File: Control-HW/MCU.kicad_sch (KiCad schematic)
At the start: 6 parts

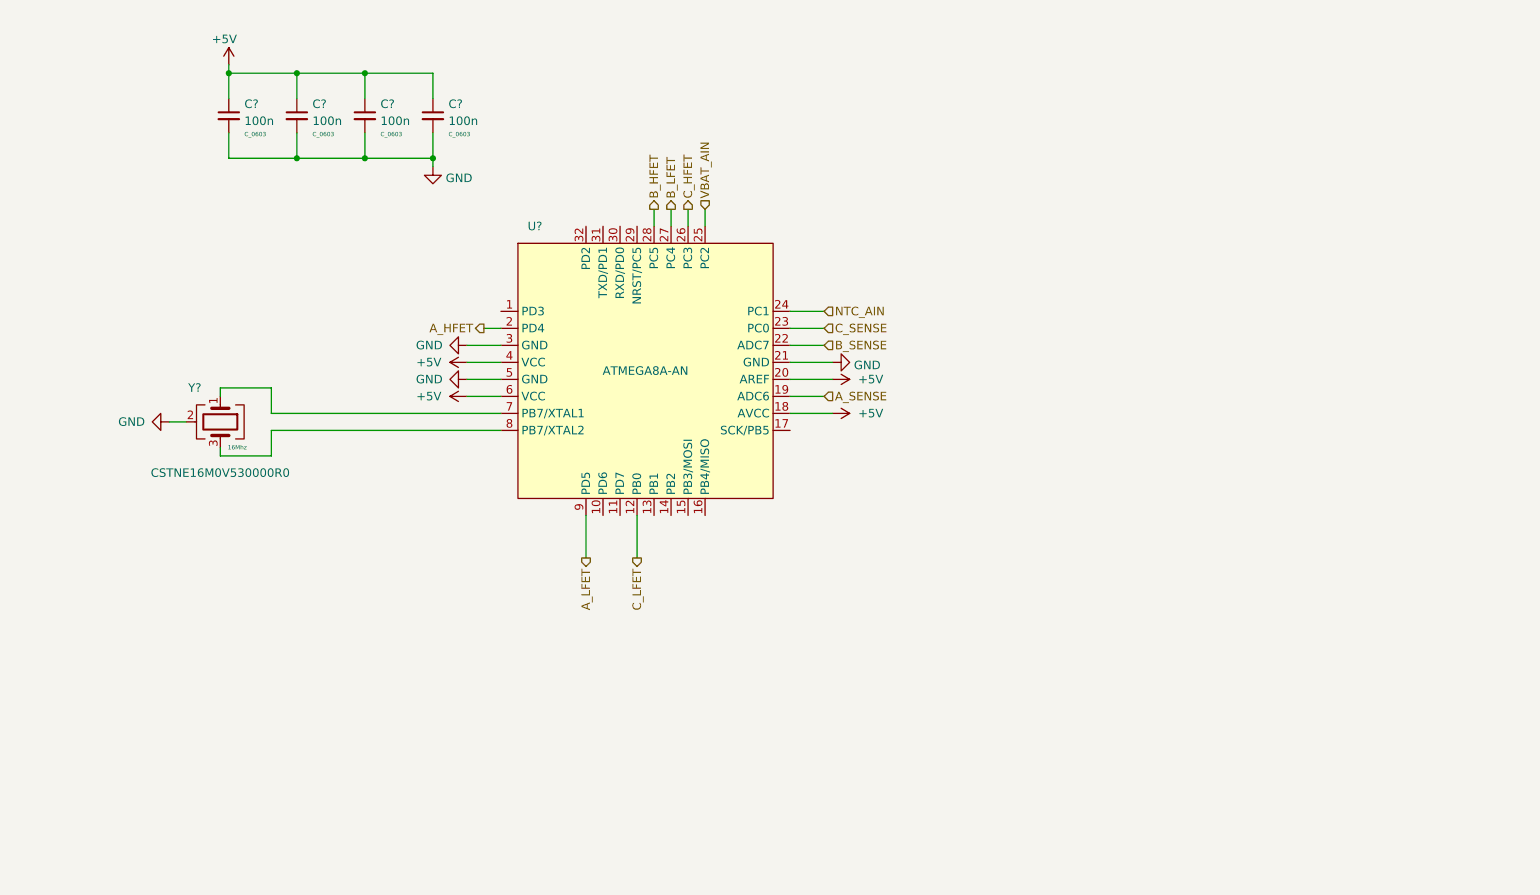
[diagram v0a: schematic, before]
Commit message: Assign pinout for MCU
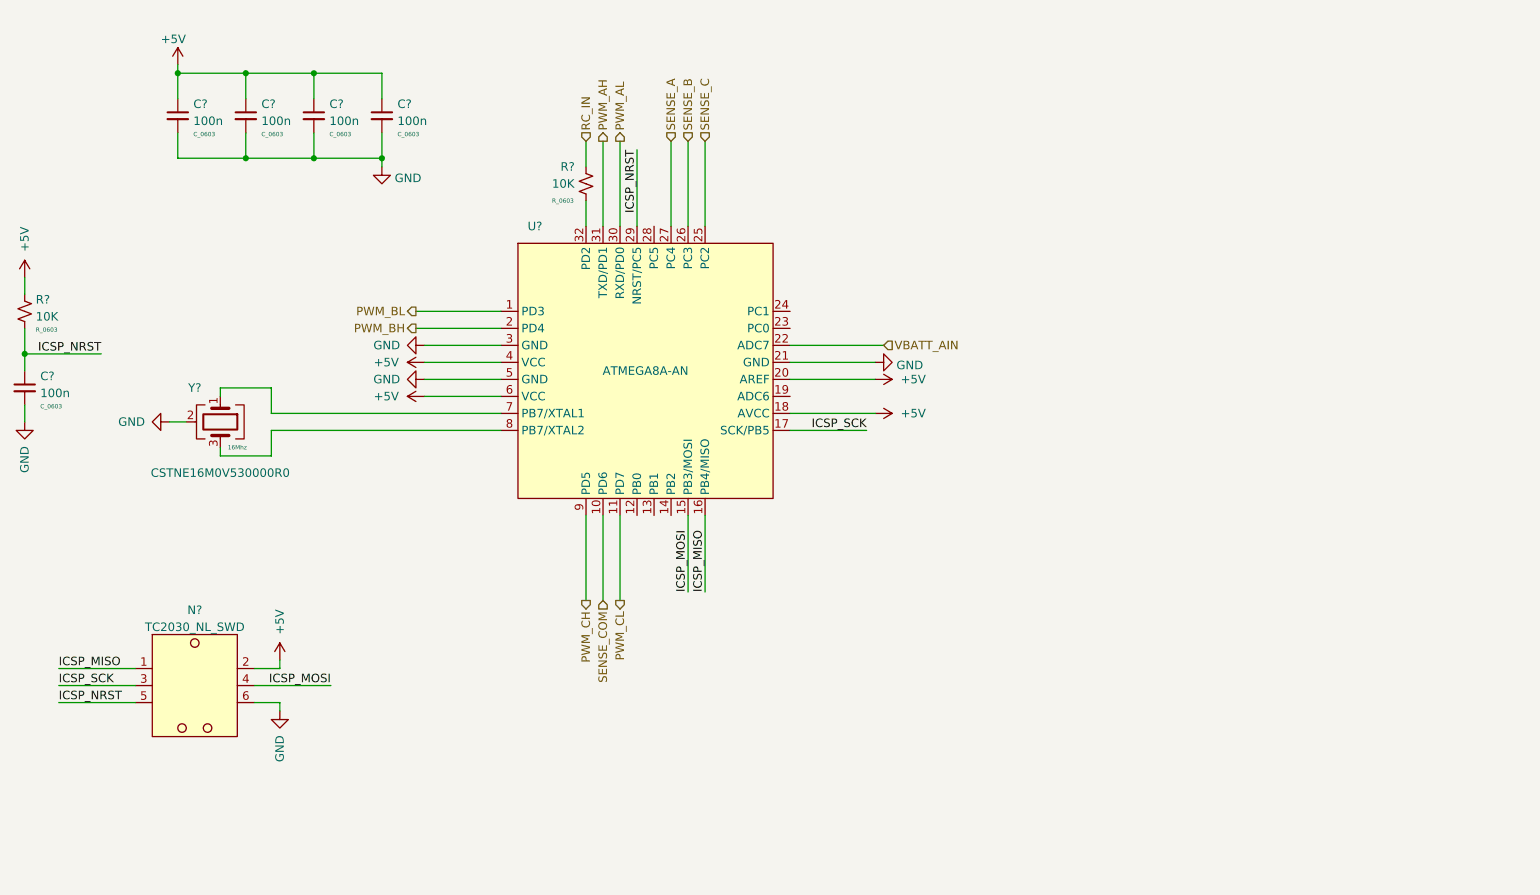
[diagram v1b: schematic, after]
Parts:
- added C?: 100n, C_Capacitor:C_0603, symbol C_Capacitor:C_0603
- added N?: TC2030_NL_SWD, N_NonPart:TagConnect_2030_NL, symbol N_NonPart:TC2030_NL_SWD
- added R? (x2): 10K, R_Resistor:R_0603, symbol R_Resistor:R_0603
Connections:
- net +5V: now also N?.2, R?.1
- net GND: now also C?.2, N?.6
- net PWM_BL: now reaches U?.1 (PD3)
- net SENSE_COM: now reaches U?.10 (PD6)
- net PWM_CL: now reaches U?.11 (PD7)
- net ICSP_MOSI: now reaches U?.15 (PB3/MOSI)
- net ICSP_MOSI: now also N?.4
- net ICSP_MISO: now reaches U?.16 (PB4/MISO)
- net ICSP_MISO: now also N?.1
- net ICSP_SCK: now reaches U?.17 (SCK/PB5)
- net ICSP_SCK: now also N?.3
- net ICSP_NRST: now reaches U?.29 (NRST/PC5)
- net ICSP_NRST: now also C?.1, N?.5, R?.2
- net PWM_AL: now reaches U?.30 (RXD/PD0)
- net PWM_AH: now reaches U?.31 (TXD/PD1)
- net at U?.32 (PD2): now also R?.2
- net A_HFET renamed PWM_BH
- net A_LFET renamed PWM_CH
- net A_SENSE: no longer names the net of U?.19 (ADC6)
- net B_HFET: no longer names the net of U?.28 (PC5)
- net B_LFET renamed SENSE_A
- net B_SENSE renamed VBATT_AIN
- net C_HFET renamed SENSE_B
- net C_LFET: no longer names the net of U?.12 (PB0)
- net C_SENSE: no longer names the net of U?.23 (PC0)
- net NTC_AIN: no longer names the net of U?.24 (PC1)
- net VBAT_AIN renamed SENSE_C
- new net RC_IN: R?.1
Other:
- moved on the sheet: C?

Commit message: First pass at control HW
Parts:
- removed C?: 100n, C_Capacitor:C_0603, symbol C_Capacitor:C_0603
- added C?: 10u, C_Capacitor:C_0805, symbol C_Capacitor:C_0805
- added C?: 100n, C_Capacitor:C_0603, symbol C_Capacitor:C_0603
- added R?: 2K, R_Resistor:R_0603, symbol R_Resistor:R_0603
- added R?: 47K, R_Resistor:R_0603, symbol R_Resistor:R_0603
- R?: value 10K -> 2K
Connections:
- net +5V: now also C?.1
- net GND: now also C?.2, C?.2, R?.2
- net VBATT_AIN: now also C?.1, R?.1, R?.2
- new net VBATT: R?.1
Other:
- note added: "4.08V @ 100V"
- moved on the sheet: C?, N?, R?, U?, Y?

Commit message: First revision
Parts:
- gave numbers to parts that had none: 13
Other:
- note added: "Pinout targeted to mirrow the rb70a.hex requirements"
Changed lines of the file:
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@@
+    (effects (font (size 1.27 1.27)) (justify left bottom))
+  )
+  (text "Pinout targeted to mirrow the rb70a.hex requirements"
+    (at 130.81 45.72 0)
     (effects (font (size 1.27 1.27)) (justify left bottom))
   )
@@
   (symbol (lib_id "power:GND") (at 46.99 101.6 0) (unit 1)
     (in_bom yes) (on_board yes)
-    (property "Reference" "#PWR?" (id 0) (at 46.99 107.95 0)
+    (property "Reference" "#PWR07" (id 0) (at 46.99 107.95 0)
       (effects (font (size 1.27 1.27)) hide)
     )
@@
   (symbol (lib_id "power:+5V") (at 46.99 80.01 0) (unit 1)
     (in_bom yes) (on_board yes)
-    (property "Reference" "#PWR?" (id 0) (at 46.99 83.82 0)
+    (property "Reference" "#PWR06" (id 0) (at 46.99 83.82 0)
       (effects (font (size 1.27 1.27)) hide)
     )
@@
   (symbol (lib_id "C_Capacitor:C_0805") (at 97.79 41.91 0) (unit 1)
     (in_bom yes) (on_board yes) (fields_autoplaced)
-    (property "Reference" "C?" (id 0) (at 100.1141 40.167 0)
+    (property "Reference" "C5" (id 0) (at 100.1141 40.167 0)
       (effects (font (size 1.27 1.27)) (justify left))
     )
@@
   (symbol (lib_id "N_NonPart:TC2030_NL_SWD") (at 69.85 147.32 0) (unit 1)
     (in_bom no) (on_board yes) (fields_autoplaced)
-    (property "Reference" "N?" (id 0) (at 69.85 136.051 0))
+    (property "Reference" "N6" (id 0) (at 69.85 136.051 0))
     (property "Value" "TC2030_NL_SWD" (id 1) (at 69.85 138.5879 0))
     (property "Footprint" "N_NonPart:TagConnect_2030_NL" (id 2) (at 69.85 158.75 0)
@@
   (symbol (lib_id "power:+5V") (at 123.19 93.98 90) (unit 1)
     (in_bom yes) (on_board yes)
-    (property "Reference" "#PWR?" (id 0) (at 127 93.98 0)
+    (property "Reference" "#PWR014" (id 0) (at 127 93.98 0)
       (effects (font (size 1.27 1.27)) hide)
     )
@@
   (symbol (lib_id "power:GND") (at 85.09 102.87 270) (unit 1)
     (in_bom yes) (on_board yes)
-    (property "Reference" "#PWR?" (id 0) (at 78.74 102.87 0)
+    (property "Reference" "#PWR011" (id 0) (at 78.74 102.87 0)
       (effects (font (size 1.27 1.27)) hide)
     )
@@
   (symbol (lib_id "power:GND") (at 228.6 99.06 0) (unit 1)
     (in_bom yes) (on_board yes)
-    (property "Reference" "#PWR?" (id 0) (at 228.6 105.41 0)
+    (property "Reference" "#PWR020" (id 0) (at 228.6 105.41 0)
       (effects (font (size 1.27 1.27)) hide)
     )
@@
   (symbol (lib_id "C_Capacitor:C_0603") (at 87.63 41.91 0) (unit 1)
     (in_bom yes) (on_board yes) (fields_autoplaced)
-    (property "Reference" "C?" (id 0) (at 89.9541 40.167 0)
+    (property "Reference" "C4" (id 0) (at 89.9541 40.167 0)
       (effects (font (size 1.27 1.27)) (justify left))
     )
@@
   (symbol (lib_id "power:+5V") (at 190.5 96.52 270) (unit 1)
     (in_bom yes) (on_board yes)
-    (property "Reference" "#PWR?" (id 0) (at 186.69 96.52 0)
+    (property "Reference" "#PWR018" (id 0) (at 186.69 96.52 0)
       (effects (font (size 1.27 1.27)) hide)
     )
@@
   (symbol (lib_id "power:+5V") (at 123.19 99.06 90) (unit 1)
     (in_bom yes) (on_board yes)
-    (property "Reference" "#PWR?" (id 0) (at 127 99.06 0)
+    (property "Reference" "#PWR016" (id 0) (at 127 99.06 0)
       (effects (font (size 1.27 1.27)) hide)
     )
@@
   (symbol (lib_id "power:GND") (at 82.55 151.13 0) (unit 1)
     (in_bom yes) (on_board yes)
-    (property "Reference" "#PWR?" (id 0) (at 82.55 157.48 0)
+    (property "Reference" "#PWR010" (id 0) (at 82.55 157.48 0)
       (effects (font (size 1.27 1.27)) hide)
     )
@@
   (symbol (lib_id "power:+5V") (at 82.55 143.51 0) (unit 1)
     (in_bom yes) (on_board yes)
-    (property "Reference" "#PWR?" (id 0) (at 82.55 147.32 0)
+    (property "Reference" "#PWR09" (id 0) (at 82.55 147.32 0)
       (effects (font (size 1.27 1.27)) hide)
     )
@@
   (symbol (lib_id "power:GND") (at 97.79 49.53 0) (unit 1)
     (in_bom yes) (on_board yes) (fields_autoplaced)
-    (property "Reference" "#PWR?" (id 0) (at 97.79 55.88 0)
+    (property "Reference" "#PWR012" (id 0) (at 97.79 55.88 0)
       (effects (font (size 1.27 1.27)) hide)
     )
@@
   (symbol (lib_id "power:GND") (at 190.5 93.98 90) (unit 1)
     (in_bom yes) (on_board yes) (fields_autoplaced)
-    (property "Reference" "#PWR?" (id 0) (at 196.85 93.98 0)
+    (property "Reference" "#PWR017" (id 0) (at 196.85 93.98 0)
       (effects (font (size 1.27 1.27)) hide)
     )
@@
   (symbol (lib_id "C_Capacitor:C_0603") (at 217.17 92.71 0) (unit 1)
     (in_bom yes) (on_board yes) (fields_autoplaced)
-    (property "Reference" "C?" (id 0) (at 219.4941 90.967 0)
+    (property "Reference" "C6" (id 0) (at 219.4941 90.967 0)
       (effects (font (size 1.27 1.27)) (justify left))
     )
@@
   (symbol (lib_id "C_Capacitor:C_0603") (at 46.99 96.52 0) (unit 1)
     (in_bom yes) (on_board yes) (fields_autoplaced)
-    (property "Reference" "C?" (id 0) (at 49.3141 94.777 0)
+    (property "Reference" "C1" (id 0) (at 49.3141 94.777 0)
       (effects (font (size 1.27 1.27)) (justify left))
     )
@@
   (symbol (lib_id "C_Capacitor:C_0603") (at 77.47 41.91 0) (unit 1)
     (in_bom yes) (on_board yes) (fields_autoplaced)
-    (property "Reference" "C?" (id 0) (at 79.7941 40.167 0)
+    (property "Reference" "C3" (id 0) (at 79.7941 40.167 0)
       (effects (font (size 1.27 1.27)) (justify left))
     )
@@
   (symbol (lib_id "power:+5V") (at 67.31 34.29 0) (unit 1)
     (in_bom yes) (on_board yes)
-    (property "Reference" "#PWR?" (id 0) (at 67.31 38.1 0)
+    (property "Reference" "#PWR08" (id 0) (at 67.31 38.1 0)
       (effects (font (size 1.27 1.27)) hide)
     )
@@
   (symbol (lib_id "R_Resistor:R_0603") (at 46.99 85.09 0) (unit 1)
     (in_bom yes) (on_board yes) (fields_autoplaced)
-    (property "Reference" "R?" (id 0) (at 48.641 83.3407 0)
+    (property "Reference" "R1" (id 0) (at 48.641 83.3407 0)
       (effects (font (size 1.27 1.27)) (justify left))
     )
@@
   (symbol (lib_id "R_Resistor:R_0603") (at 147.32 67.31 0) (unit 1)
     (in_bom yes) (on_board yes)
-    (property "Reference" "R?" (id 0) (at 142.875 65.405 0)
+    (property "Reference" "R2" (id 0) (at 142.875 65.405 0)
       (effects (font (size 1.27 1.27)) (justify left))
     )
@@
   (symbol (lib_id "Y_Oscillator:CSTNE16M0V530000R0") (at 92.71 102.87 270) (unit 1)
     (in_bom yes) (on_board yes)
-    (property "Reference" "Y?" (id 0) (at 88.9 97.79 90))
+    (property "Reference" "Y1" (id 0) (at 88.9 97.79 90))
     (property "Value" "CSTNE16M0V530000R0" (id 1) (at 92.71 110.49 90))
     (property "Footprint" "Y_Oscillator:Oscillator_SMD3_3.2x1.3" (id 2) (at 80.01 102.87 0)
@@
   (symbol (lib_id "C_Capacitor:C_0603") (at 67.31 41.91 0) (unit 1)
     (in_bom yes) (on_board yes) (fields_autoplaced)
-    (property "Reference" "C?" (id 0) (at 69.6341 40.167 0)
+    (property "Reference" "C2" (id 0) (at 69.6341 40.167 0)
       (effects (font (size 1.27 1.27)) (justify left))
     )
@@
   (symbol (lib_id "R_Resistor:R_0603") (at 228.6 92.71 0) (unit 1)
     (in_bom yes) (on_board yes) (fields_autoplaced)
-    (property "Reference" "R?" (id 0) (at 230.251 90.9607 0)
+    (property "Reference" "R4" (id 0) (at 230.251 90.9607 0)
       (effects (font (size 1.27 1.27)) (justify left))
     )
@@
   (symbol (lib_id "power:GND") (at 123.19 91.44 270) (unit 1)
     (in_bom yes) (on_board yes)
-    (property "Reference" "#PWR?" (id 0) (at 116.84 91.44 0)
+    (property "Reference" "#PWR013" (id 0) (at 116.84 91.44 0)
       (effects (font (size 1.27 1.27)) hide)
     )
@@
   (symbol (lib_id "power:+5V") (at 190.5 101.6 270) (unit 1)
     (in_bom yes) (on_board yes)
-    (property "Reference" "#PWR?" (id 0) (at 186.69 101.6 0)
+    (property "Reference" "#PWR019" (id 0) (at 186.69 101.6 0)
       (effects (font (size 1.27 1.27)) hide)
     )
@@
   (symbol (lib_id "power:GND") (at 123.19 96.52 270) (unit 1)
     (in_bom yes) (on_board yes)
-    (property "Reference" "#PWR?" (id 0) (at 116.84 96.52 0)
+    (property "Reference" "#PWR015" (id 0) (at 116.84 96.52 0)
       (effects (font (size 1.27 1.27)) hide)
     )
@@
   (symbol (lib_id "U_MCU:ATMEGA8A-AN") (at 137.16 114.3 0) (unit 1)
     (in_bom yes) (on_board yes)
-    (property "Reference" "U?" (id 0) (at 139.7 73.66 0))
+    (property "Reference" "U1" (id 0) (at 139.7 73.66 0))
     (property "Value" "ATMEGA8A-AN" (id 1) (at 156.21 95.25 0))
     (property "Footprint" "U_IC:LQFP32_08_7x7" (id 2) (at 156.21 129.54 0)
@@
   (symbol (lib_id "R_Resistor:R_0603") (at 228.6 82.55 0) (unit 1)
     (in_bom yes) (on_board yes) (fields_autoplaced)
-    (property "Reference" "R?" (id 0) (at 230.251 80.8007 0)
-      (effects (font (size 1.27 1.27)) (justify left))
-    )
+    (property "Reference" "R3" (id 0) (at 230.251 80.8007 0)
+      (effects (font (size 1.27 1.27)) (justify left))
+    )

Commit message: Add fp-info to gitignore
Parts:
- N6: footprint N_NonPart:TagConnect_2030_NL -> N_NonPart:TagConnect_TC2030_NL
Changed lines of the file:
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@@
     (property "Reference" "N6" (id 0) (at 69.85 136.051 0))
     (property "Value" "TC2030_NL_SWD" (id 1) (at 69.85 138.5879 0))
-    (property "Footprint" "N_NonPart:TagConnect_2030_NL" (id 2) (at 69.85 158.75 0)
+    (property "Footprint" "N_NonPart:TagConnect_TC2030_NL" (id 2) (at 69.85 158.75 0)
       (effects (font (size 1.27 1.27)) hide)
     )
